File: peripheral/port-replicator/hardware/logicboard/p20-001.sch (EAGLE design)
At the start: 25 parts, among them IC1 74LS07N, J0 DC9V, J11 AUDIO_JACK_3.5MM_PTH, J12 AUDIO_JACK_3.5MM_PTH, J13 AUDIO_JACK_3.5MM_PTH, J14 AUDIO_JACK_3.5MM_PTH, J21 DIN5, J22 DIN5, J23 DIN5, X0 MKDSN1,5/2-5,08

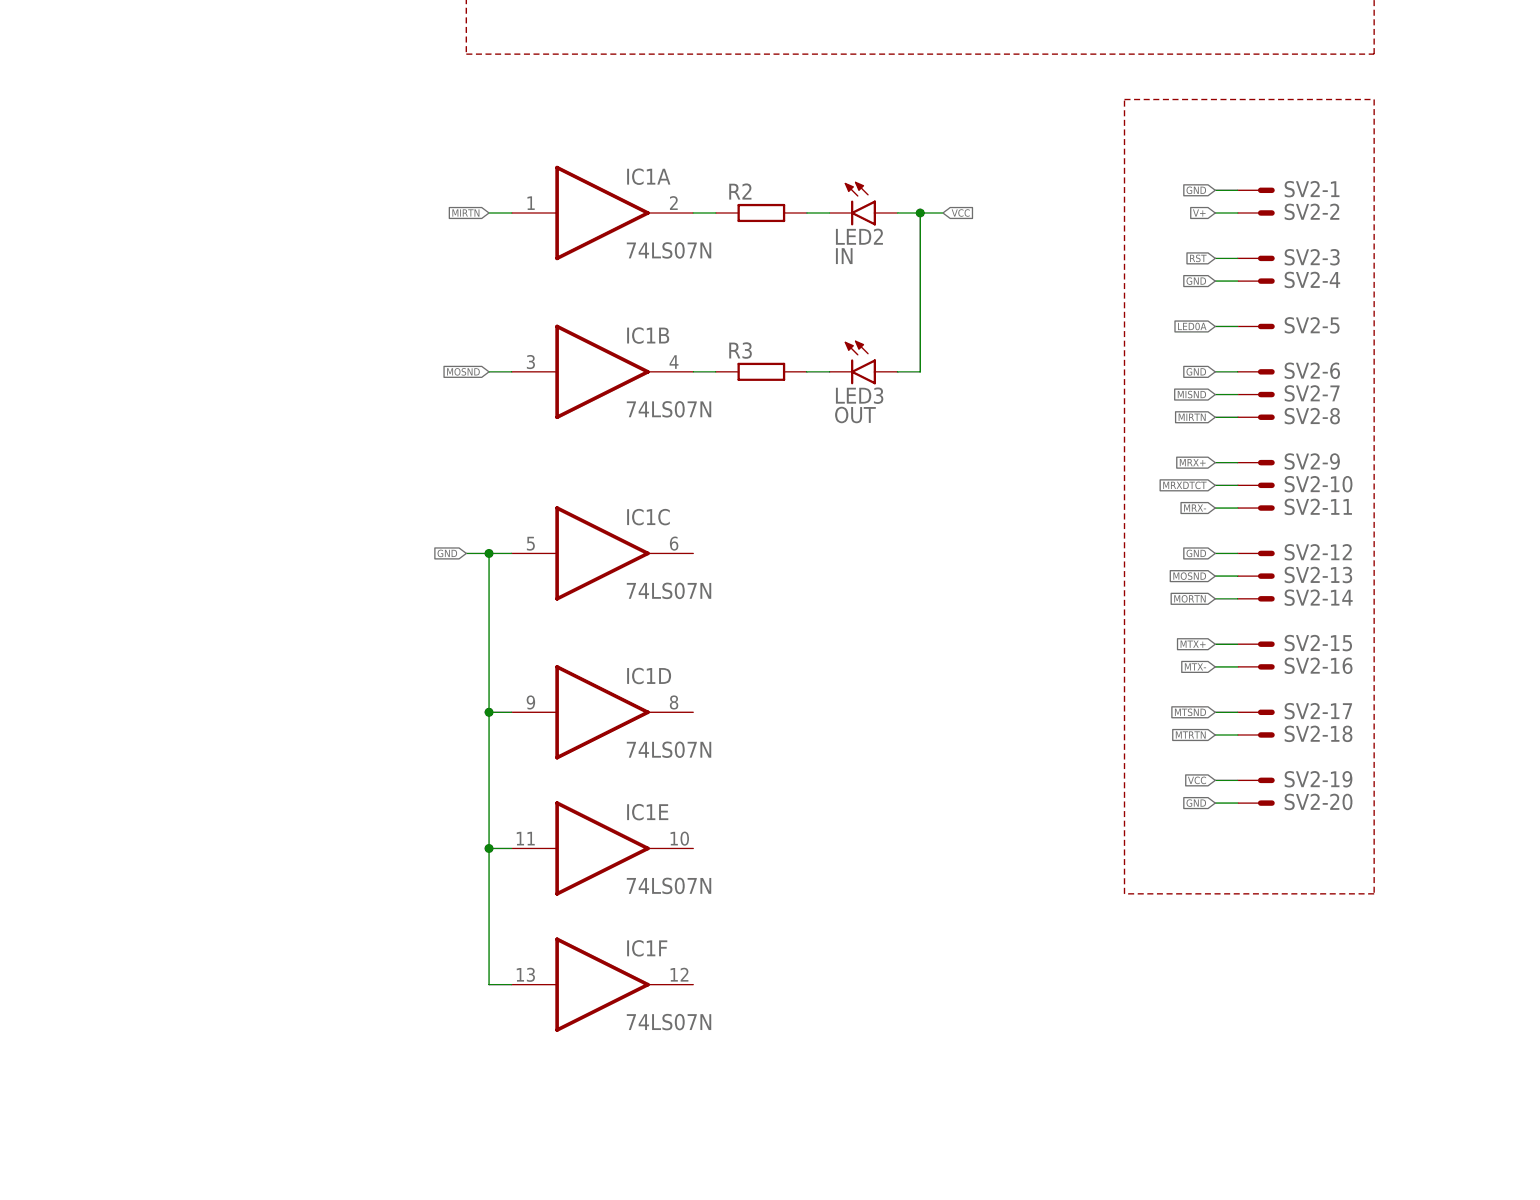
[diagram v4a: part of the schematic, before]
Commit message: Updated backside port to 2.0.
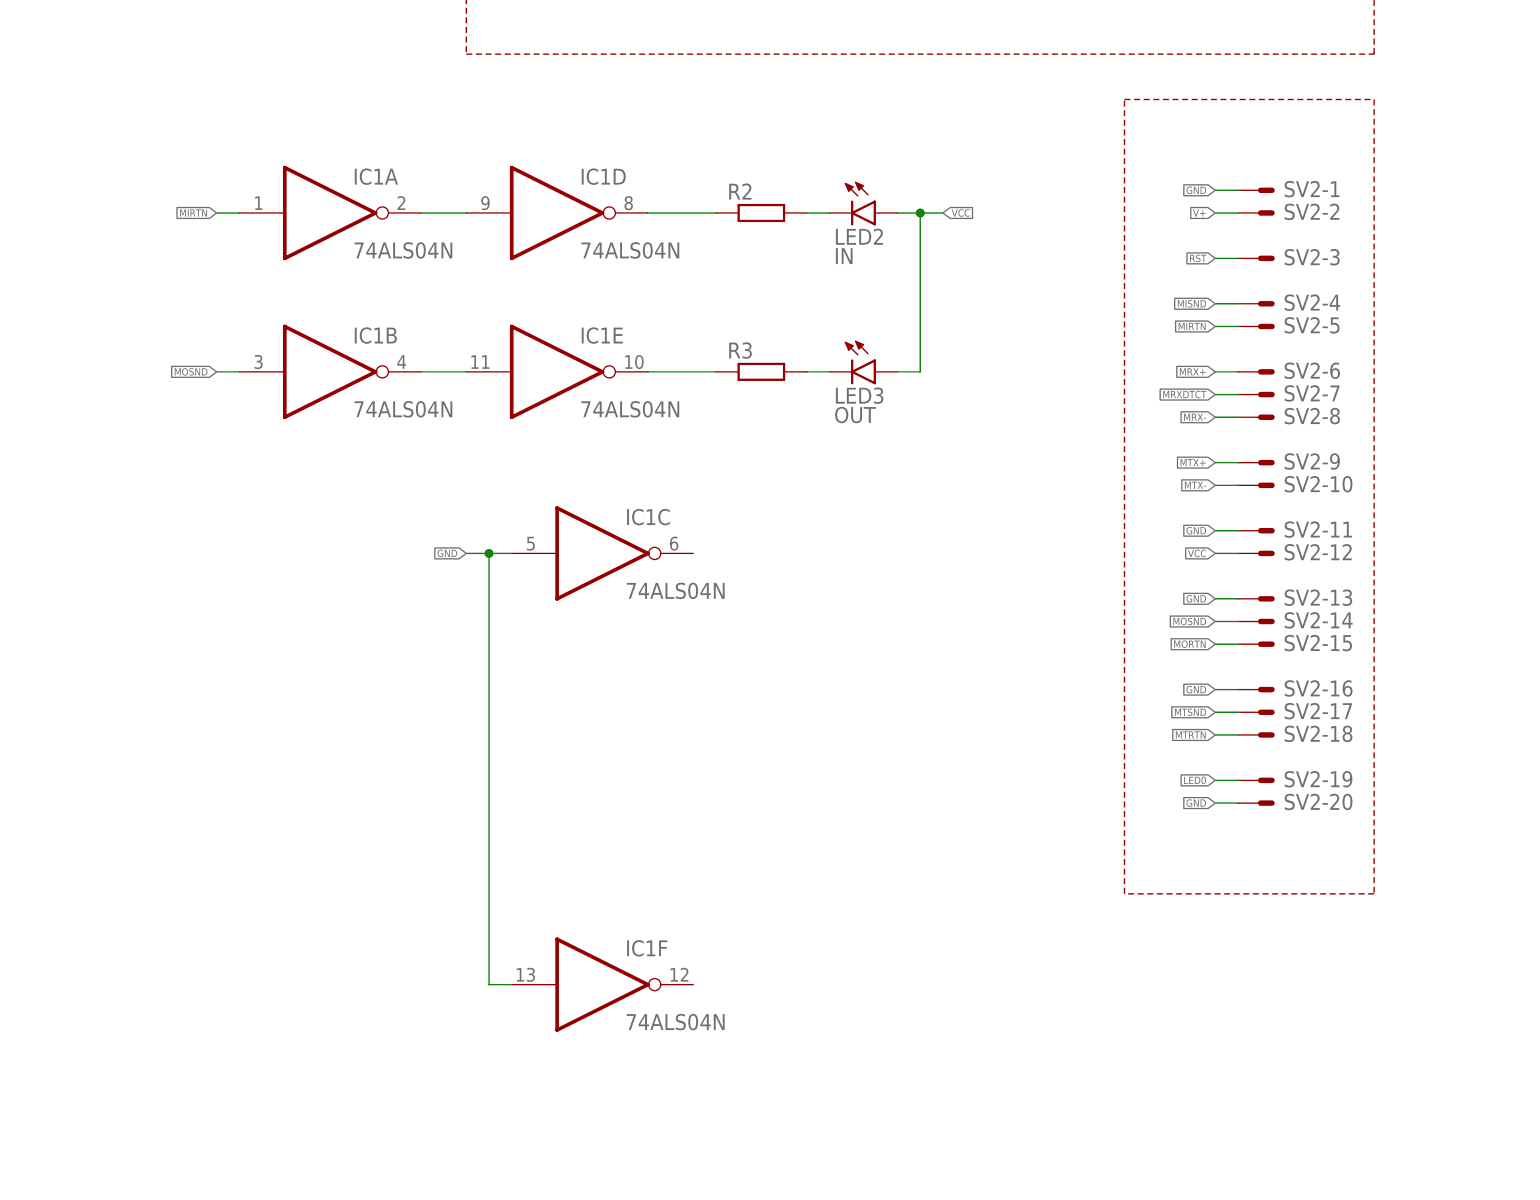
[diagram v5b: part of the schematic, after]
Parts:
- IC1: value 74LS07N -> 74ALS04N; device 74xx-us:74LS07N -> 74xx-us:74ALS04N
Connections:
- removed net LED0A: SV2-5.S
- new net N$3: IC1D.O, R2.1
- new net N$4: IC1E.O, R3.1
- net GND: now also SV2-11.S, SV2-13.S, SV2-16.S; no longer IC1D.I, IC1E.I, SV2-12.S, SV2-4.S, SV2-6.S
- net LED0: now also SV2-19.S
- net MIRTN: now also SV2-5.S; no longer SV2-8.S
- net MISND: now also SV2-4.S; no longer SV2-7.S
- net MORTN: now also SV2-15.S; no longer SV2-14.S
- net MOSND: now also SV2-14.S; no longer SV2-13.S
- net MRX+: now also SV2-6.S; no longer SV2-9.S
- net MRX-: now also SV2-8.S; no longer SV2-11.S
- net MRXDTCT: now also SV2-7.S; no longer SV2-10.S
- net MTX+: now also SV2-9.S; no longer SV2-15.S
- net MTX-: now also SV2-10.S; no longer SV2-16.S
- net N$1: now also IC1D.I; no longer R2.1
- net N$2: now also IC1E.I; no longer R3.1
- net VCC: now also SV2-12.S; no longer SV2-19.S
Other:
- moved on the sheet: SV2-11, SV2-13, SV2-14, SV2-16, SV2-4

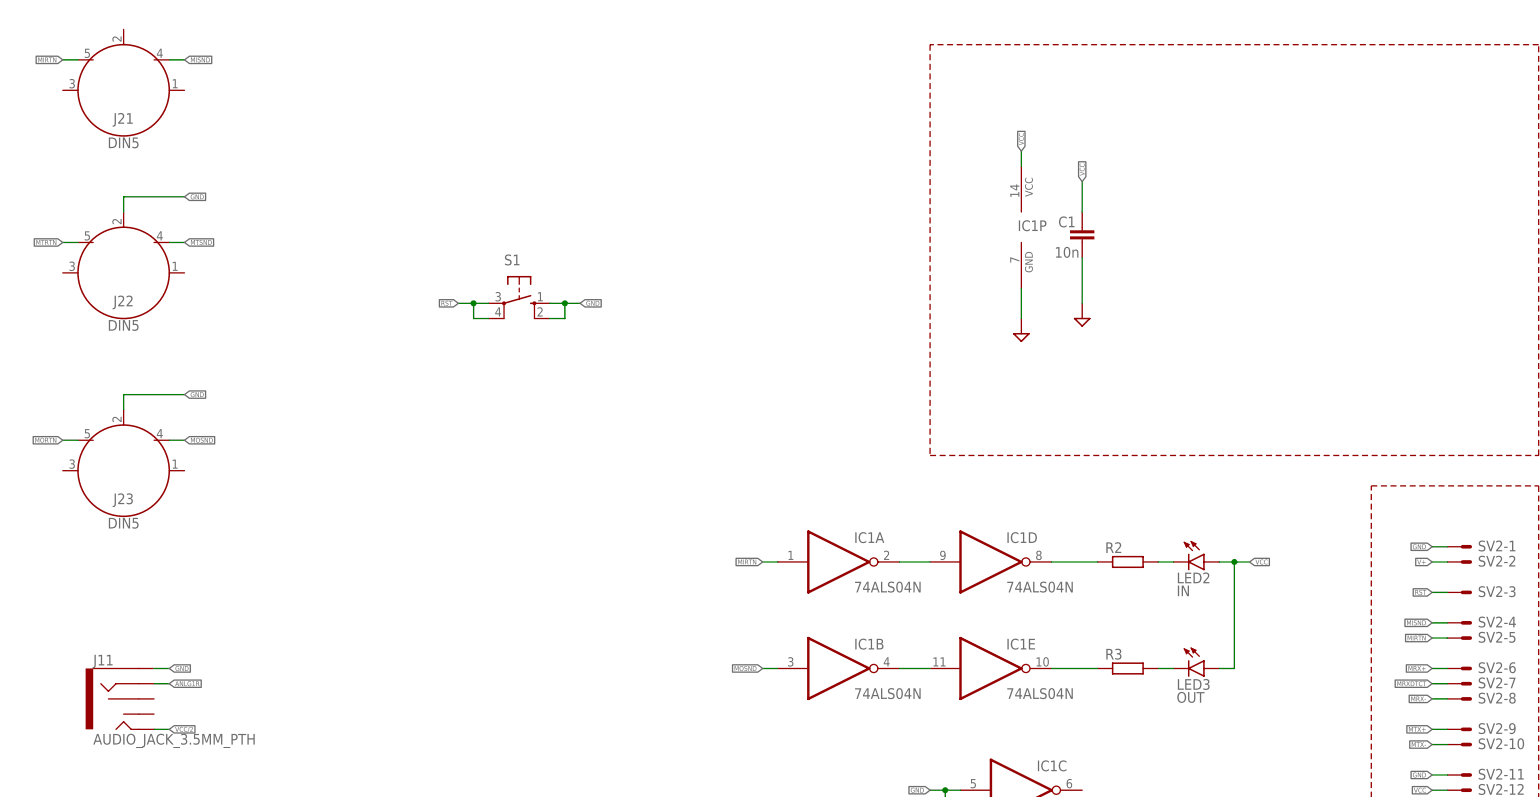
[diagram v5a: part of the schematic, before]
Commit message: Renumbered parts of Port Replicator.
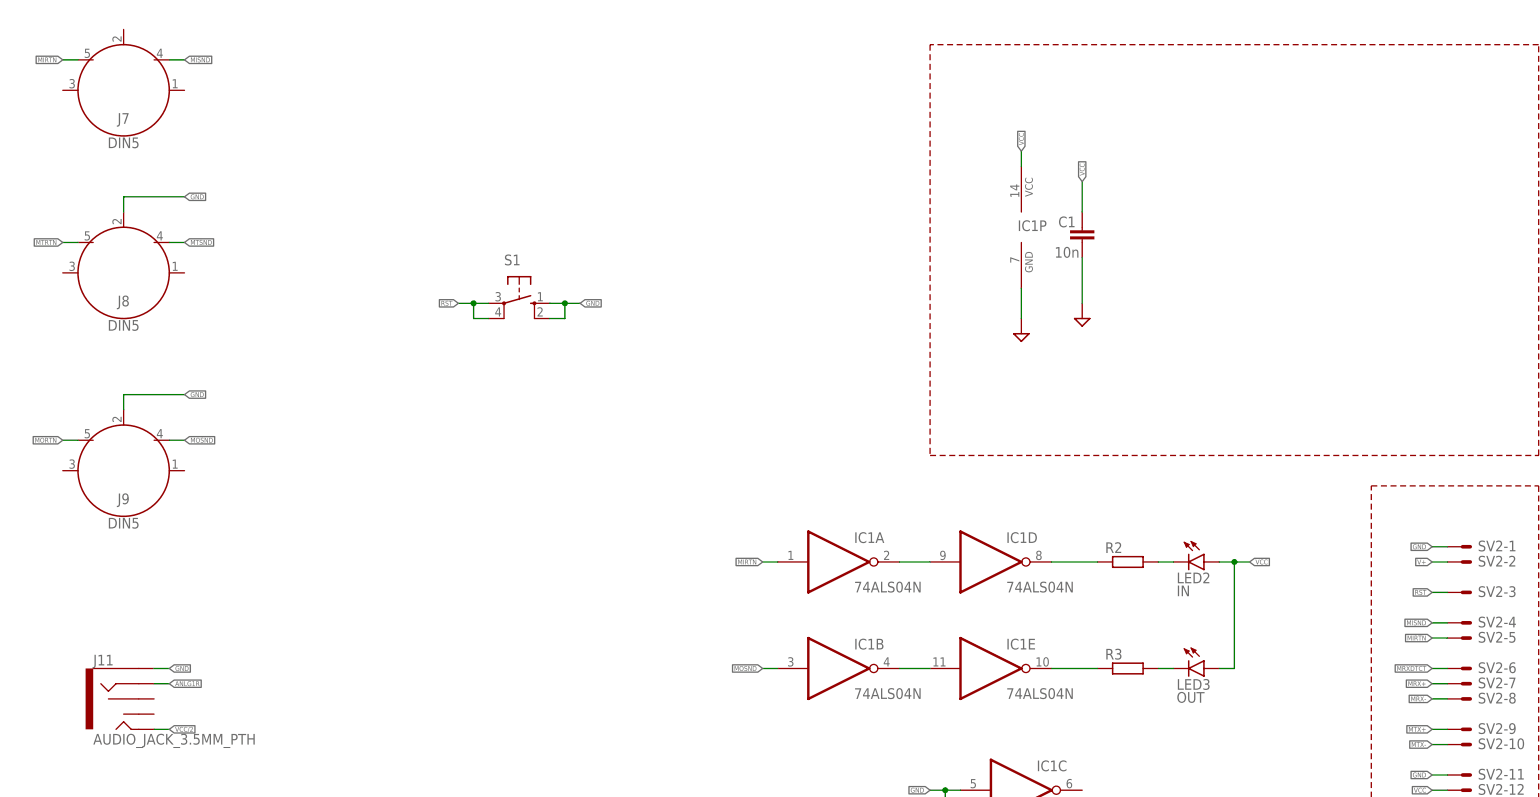
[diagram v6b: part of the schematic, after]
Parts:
- renumbered J21 to J7, J22 to J8, J23 to J9
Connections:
- net MRX+: now also SV2-7.S; no longer SV2-6.S
- net MRXDTCT: now also SV2-6.S; no longer SV2-7.S
